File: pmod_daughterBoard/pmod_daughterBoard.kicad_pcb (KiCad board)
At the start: 2 copper layers, 36.8 x 68.6 mm, 17 parts, among them J1 Conn_02x04_Odd_Even, J11 Conn_02x06_Odd_Even, J2 Conn_02x04_Odd_Even, J3 Conn_Coaxial, J4 Conn_01x02_Male, Q1 N/A

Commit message: update board
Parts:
- removed the J1 at (166.1, 56.4)
- removed the J2 at (183.1, 56.4)
- removed J4: Conn_01x02_Male, Connector_PinSocket_2.54mm:PinSocket_1x02_P2.54mm_Vertical
- removed the R10 at (168.1, 69.1)
- added J3: Conn_02x09_Odd_Even, Connector_PinHeader_2.54mm:PinHeader_2x09_P2.54mm_Vertical, F.Cu at (182.9, 50.8)
- J2: renamed from J3; footprint pmod_daughterBoard:LINX_CONSMA001-SMD-G-T -> Connector_Coaxial:SMA_Amphenol_132291-12_Vertical
- REF**: value MountingHole_5.3mm_M5 -> MountingHole_3.2mm_M3; footprint MountingHole:MountingHole_5.3mm_M5 -> MountingHole:MountingHole_3.2mm_M3
- moved R1 29.5 mm to (182.9, 48.3), turned to 90 degrees
- moved R2 26.0 mm to (180.3, 48.3), turned to 90 degrees
- moved R8 24.8 mm to (165.1, 48.3), turned to 90 degrees
- moved R7 23.5 mm to (167.6, 48.3), turned to 90 degrees
- moved R6 22.6 mm to (170.2, 48.3), turned to 90 degrees
- moved R3 22.5 mm to (177.8, 48.3), turned to 90 degrees
- moved R5 22.3 mm to (172.7, 48.3), turned to 90 degrees
- moved R4 19.1 mm to (175.3, 48.3), turned to 90 degrees
- moved Q1 17.1 mm to (180.6, 59.2), turned to 180 degrees
- moved R10 11.7 mm to (176.8, 60.2), turned to 0 degrees
- moved REF** 11.4 mm to (173.7, 82.5)
- moved J2 10.5 mm to (173.2, 69.3)
- moved J1 0.92 mm to (179.1, 43.2)
- renumbered J11 to J1, R9 to R10
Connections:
- net Net-(J1-Pad8) renamed GPIO1
- net Net-(J11-Pad6) renamed GPIO6
- J1 pad 2: Net-(J11-Pad2) -> GPIO2
- J1 pad 3: Net-(J1-Pad6) -> GPIO3
- J1 pad 4: Net-(J11-Pad4) -> GPIO4
- J1 pad 5: Net-(J1-Pad4) -> GPIO5
- J1 pad 7: Net-(J1-Pad2) -> GPIO7
- J1 pad 8: Net-(J11-Pad8) -> GPIO8
- R2 pad 1: Net-(J1-Pad6) -> GPIO2
- R3 pad 1: Net-(J1-Pad4) -> GPIO3
- R4 pad 1: Net-(J1-Pad2) -> GPIO4
- R5 pad 1: Net-(J11-Pad8) -> GPIO5
- R7 pad 1: Net-(J11-Pad4) -> GPIO7
- R8 pad 1: Net-(J11-Pad2) -> GPIO8
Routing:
- net Net-(J11-Pad8): track 33.9 -> 0.00 mm
- net Net-(J1-Pad6): track 30.7 -> 0.00 mm
- net GPIO1: track 45.2 -> 18.7 mm
- net Net-(J11-Pad4): track 26.1 -> 0.00 mm
- net Net-(J1-Pad4): track 26.0 -> 0.00 mm
- net Net-(J11-Pad2): track 22.6 -> 0.00 mm
- net Net-(J1-Pad2): track 22.4 -> 0.00 mm
- net +3V3: track 44.7 -> 24.6 mm
- net GPIO6: track 30.4 -> 12.0 mm
- net GPIO8: track 0.00 -> 13.8 mm
- net GPIO2: track 0.00 -> 11.8 mm
- net GPIO4: track 0.00 -> 11.3 mm
- net GPIO7: track 0.00 -> 9.22 mm
- net GPIO5: track 0.00 -> 8.44 mm
- net GPIO3: track 0.00 -> 8.14 mm
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- removed copper zone on F.Cu, net GND
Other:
- board size 36.8 x 68.6 mm -> 25.4 x 52.1 mm
- net class Default removed
- board text removed: "0"
- board text removed: "1"
- board text removed: "12"
- board text removed: "13"
- board text removed: "2"
- board text removed: "3"
- board text removed: "4"
- board text removed: "5"
- board text removed: "6"
- board text removed: "7"

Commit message: began implementation of various gpio inputs. Removed redundant GND resistor
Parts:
- J2: footprint Connector_Coaxial:SMA_Amphenol_132291-12_Vertical -> pmod_daughterBoard:LINX_CONSMA001-SMD-G-T
- R2: value 2K -> 2k
- moved R2 9.00 mm to (177.8, 56.9), turned to 0 degrees
- moved J2 6.91 mm to (180.1, 69.3)
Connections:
- R2 pad 2: GND -> +3V3
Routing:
- net GPIO2: track 11.8 -> 19.1 mm
- net Net-(J2-Pad1): track 10.4 -> 12.0 mm
- net +3V3: track 24.6 -> 25.6 mm
- net GND: track 7.10 -> 6.08 mm, vias 7 -> 6

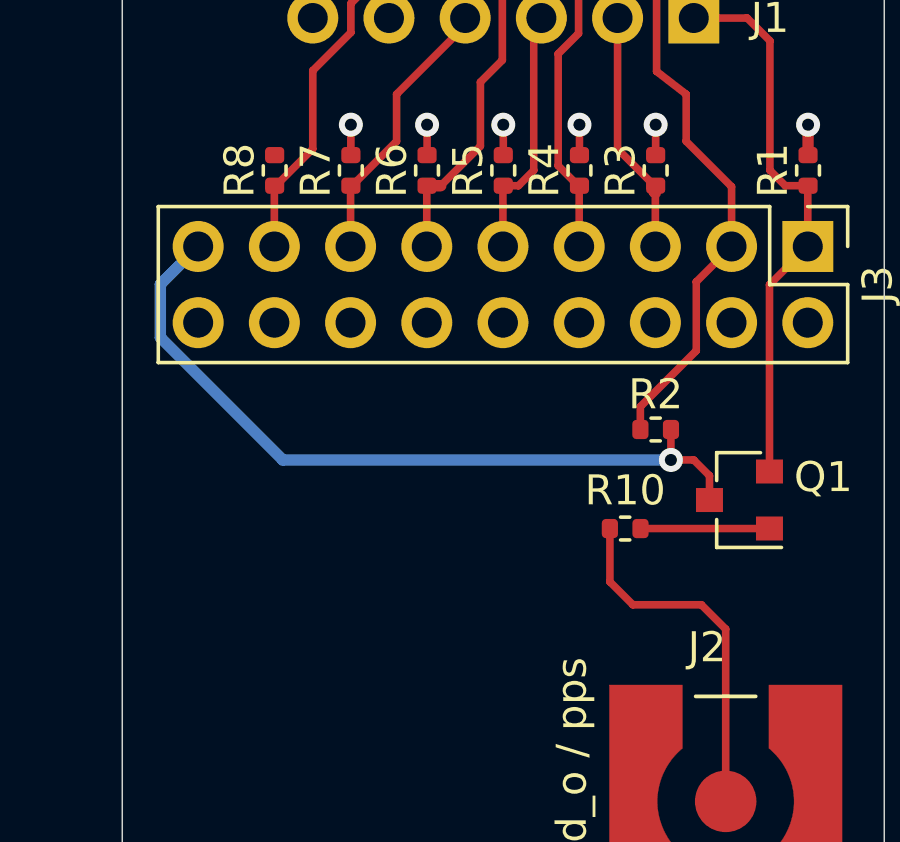
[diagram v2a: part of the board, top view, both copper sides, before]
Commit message: implemented differential pair receiver on pmod board
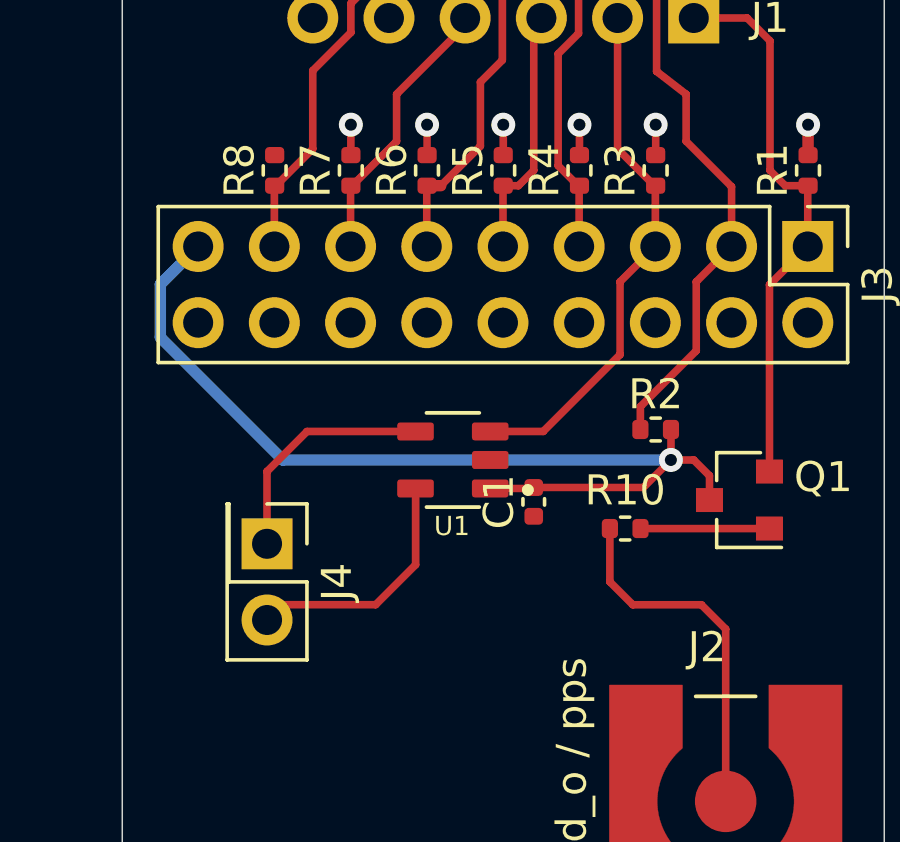
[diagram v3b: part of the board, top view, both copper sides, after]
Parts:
- added C1: 0.1uF, Capacitor_SMD:C_0402_1005Metric, F.Cu at (173.7, 59.3)
- added J4: Conn_02x01, Connector_PinHeader_2.54mm:PinHeader_2x01_P2.54mm_Vertical, F.Cu at (164.8, 60.7)
- added U1: MAX3280EAUK, max3280:SOT95P280X145-5N, F.Cu at (171.0, 57.9)
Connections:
- J3 pad 17: +3V3 -> unconnected-(J3-Pad17)
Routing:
- net GPIO3: track 8.14 -> 17.4 mm
- net TOV-IN-: track 0.00 -> 8.81 mm
- net TOV-IN+: track 0.00 -> 8.13 mm
- net +3V3: track 25.6 -> 32.0 mm

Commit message: updated
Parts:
- moved C1 0.76 mm to (174.5, 59.3)
- moved R3 0.51 mm to (177.8, 47.8)
- moved R4 0.51 mm to (175.3, 47.8)
- moved R5 0.51 mm to (172.7, 47.8)
- moved R6 0.51 mm to (170.2, 47.8)
- moved R7 0.51 mm to (167.6, 47.8)
- moved R8 0.51 mm to (165.1, 47.8)
- moved R1 0.38 mm to (182.9, 47.9)
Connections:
- J3 pad 17: unconnected-(J3-Pad17) -> +3V3
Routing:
- net +3V3: track 32.0 -> 43.8 mm
- net Net-(J2-Pad1): track 12.0 -> 10.7 mm
- net GND: track 6.08 -> 7.23 mm, vias 6 -> 19
- net TOV-IN-: track 8.81 -> 7.91 mm
- added copper zone on F.Cu, net GND
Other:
- board text added: "TOV-IN+"
- board text added: "TOV-IN-"
